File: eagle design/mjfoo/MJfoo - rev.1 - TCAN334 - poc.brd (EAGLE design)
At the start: 35 x 35 mm, 19 parts, among them IC202 LDK320AM33R, IC302 STM32F042G6U6, IC401 TCAN334, J1 CAN, J2 Power Supply

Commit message: - updated MJfoo to rev. 1a
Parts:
- added 3V3: 3V3, pinhead:1X02
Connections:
- net 3V3: now also 3V3.2
- net GND: now also 3V3.1
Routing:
- net 3V3: track 39.9 -> 46.0 mm
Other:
- board text added: "MJfoo POC ejovrh rev.1a"
- board text removed: "MJfoo POC ejovrh rev.1"
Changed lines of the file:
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@@
 <wire x1="32" y1="32" x2="3" y2="32" width="0.1524" layer="49"/>
 <text x="4" y="9.25" locked="yes" size="1" layer="29" font="vector" ratio="12" rot="R90" align="center">MJfoo POC
-ejovrh rev.1</text>
+ejovrh rev.1a</text>
 <wire x1="34" y1="32" x2="34" y2="3" width="2" layer="29" locked="yes"/>
 <wire x1="34" y1="3" x2="32" y2="1" width="2" layer="29" curve="-90" locked="yes"/>
@@
 <attribute name="VALUE" x="27.54" y="32.925" size="1.27" layer="27" rot="R180"/>
 </element>
+<element name="3V3" library="pinhead" library_urn="urn:adsk.eagle:library:325" package="1X02" package3d_urn="urn:adsk.eagle:package:22435/2" value="3V3" x="13" y="27" smashed="yes" rot="R270">
+<attribute name="NAME" x="13" y="23.75" size="1" layer="25" align="center"/>
+<attribute name="POPULARITY" value="98" x="13" y="27" size="1.778" layer="27" rot="R270" display="off"/>
+<attribute name="VALUE" x="9.825" y="29.54" size="1.27" layer="27" rot="R270"/>
+</element>
 </elements>
 <signals>
@@
 <contactref element="C401" pad="2"/>
 <via x="8.875" y="24.875" extent="1-16" drill="0.35"/>
+<contactref element="3V3" pad="1"/>
 </signal>
 <signal name="BAT+" class="1">
@@
 <wire x1="9.125" y1="22.88" x2="12.975" y2="22.88" width="0.25" layer="16"/>
 <wire x1="9.125" y1="22.025" x2="9.125" y2="22.88" width="0.25" layer="16"/>
-<wire x1="12.975" y1="20.875" x2="12.975" y2="22.75" width="0.25" layer="16"/>
-<wire x1="12.975" y1="22.75" x2="12.975" y2="22.88" width="0.25" layer="16"/>
+<wire x1="12.975" y1="20.875" x2="12.975" y2="22.88" width="0.25" layer="16"/>
 <wire x1="18.65" y1="24.98" x2="18.75" y2="24.88" width="0.25" layer="16"/>
 <wire x1="18.75" y1="24.88" x2="18.75" y2="22.88" width="0.25" layer="16"/>
@@
 <wire x1="18.65" y1="25.08" x2="18.75" y2="24.98" width="0.25" layer="1"/>
 <wire x1="18.65" y1="24.98" x2="18.75" y2="24.98" width="0.25" layer="16"/>
-<wire x1="12.975" y1="22.75" x2="12.975" y2="22.75" width="0.25" layer="16"/>
+<contactref element="3V3" pad="2"/>
+<wire x1="13" y1="25.73" x2="13.275" y2="26.005" width="0.25" layer="1"/>
+<wire x1="18.45" y1="25.33" x2="17.775" y2="26.005" width="0.25" layer="1"/>
+<wire x1="18.45" y1="25.33" x2="18.45" y2="25.08" width="0.25" layer="1"/>
+<wire x1="13.275" y1="26.005" x2="17.775" y2="26.005" width="0.25" layer="1"/>
 </signal>
 <signal name="SYS_SWDIO" class="3">

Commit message: - unified values of passive elements to a common format
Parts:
- C202: value 1μF / 10V -> 1uF / 10V
- C207: value 1μF -> 1uF / 10V
- C301, C305, C307: value 0.1u -> 0.1uF / 10V
- C304: value 1u -> 1uF / 10V
- C401: value 47nF -> 47nF / 10V
- C405: value 0.1μF -> 0.1uF / 10V
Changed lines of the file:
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@@
 </autorouter>
 <elements>
-<element name="C202" library="rcl" library_urn="urn:adsk.eagle:library:334" package="C0402" package3d_urn="urn:adsk.eagle:package:23626/2" value="1μF / 10V" x="18" y="27.48" locked="yes" smashed="yes" rot="MR0">
+<element name="C202" library="rcl" library_urn="urn:adsk.eagle:library:334" package="C0402" package3d_urn="urn:adsk.eagle:package:23626/2" value="1uF / 10V" x="18" y="27.48" locked="yes" smashed="yes" rot="MR0">
 <attribute name="NAME" x="18" y="28.48" locked="yes" size="0.5" layer="26" rot="MR0" align="center"/>
 <attribute name="POPULARITY" value="18" x="18" y="27.48" locked="yes" size="1.778" layer="28" rot="MR0" display="off"/>
@@
 <attribute name="VALUE" x="18" y="27.48" locked="yes" size="1.27" layer="28" rot="MR0"/>
 </element>
-<element name="C207" library="rcl" library_urn="urn:adsk.eagle:library:334" package="C0402" package3d_urn="urn:adsk.eagle:package:23626/2" value="1μF" x="18" y="24.98" locked="yes" smashed="yes" rot="MR180">
+<element name="C207" library="rcl" library_urn="urn:adsk.eagle:library:334" package="C0402" package3d_urn="urn:adsk.eagle:package:23626/2" value="1uF / 10V" x="18" y="24.98" locked="yes" smashed="yes" rot="MR180">
 <attribute name="NAME" x="18" y="23.98" locked="yes" size="0.5" layer="26" rot="MR180" align="center"/>
 <attribute name="POPULARITY" value="18" x="18" y="24.98" locked="yes" size="1.778" layer="28" rot="MR180" display="off"/>
@@
 <attribute name="VALUE" x="18" y="24.98" locked="yes" size="1.27" layer="28" rot="MR180"/>
 </element>
-<element name="C301" library="rcl" library_urn="urn:adsk.eagle:library:334" package="C0402" package3d_urn="urn:adsk.eagle:package:23626/2" value="0.1u" x="13.625" y="20.875" locked="yes" smashed="yes" rot="MR0">
+<element name="C301" library="rcl" library_urn="urn:adsk.eagle:library:334" package="C0402" package3d_urn="urn:adsk.eagle:package:23626/2" value="0.1uF / 10V" x="13.625" y="20.875" locked="yes" smashed="yes" rot="MR0">
 <attribute name="NAME" x="13.625" y="21.875" locked="yes" size="0.5" layer="26" rot="MR0" align="center"/>
 <attribute name="POPULARITY" value="18" x="13.625" y="20.875" locked="yes" size="1.778" layer="28" rot="MR0" display="off"/>
@@
 <attribute name="VALUE" x="13.625" y="20.875" locked="yes" size="1.27" layer="28" rot="MR0"/>
 </element>
-<element name="C304" library="rcl" library_urn="urn:adsk.eagle:library:334" package="C0402" package3d_urn="urn:adsk.eagle:package:23626/2" value="1u" x="21.75" y="20" locked="yes" smashed="yes" rot="MR0">
+<element name="C304" library="rcl" library_urn="urn:adsk.eagle:library:334" package="C0402" package3d_urn="urn:adsk.eagle:package:23626/2" value="1uF / 10V" x="21.75" y="20" locked="yes" smashed="yes" rot="MR0">
 <attribute name="NAME" x="21.75" y="21" locked="yes" size="0.5" layer="26" rot="MR0" align="center"/>
 <attribute name="POPULARITY" value="18" x="21.75" y="20" locked="yes" size="1.778" layer="28" rot="MR0" display="off"/>
@@
 <attribute name="VALUE" x="21.75" y="20" locked="yes" size="1.27" layer="28" rot="MR0"/>
 </element>
-<element name="C305" library="rcl" library_urn="urn:adsk.eagle:library:334" package="C0402" package3d_urn="urn:adsk.eagle:package:23626/2" value="0.1u" x="13.625" y="19.625" locked="yes" smashed="yes" rot="MR0">
+<element name="C305" library="rcl" library_urn="urn:adsk.eagle:library:334" package="C0402" package3d_urn="urn:adsk.eagle:package:23626/2" value="0.1uF / 10V" x="13.625" y="19.625" locked="yes" smashed="yes" rot="MR0">
 <attribute name="NAME" x="13.625" y="18.625" locked="yes" size="0.5" layer="26" rot="MR0" align="center"/>
 <attribute name="POPULARITY" value="18" x="13.625" y="19.625" locked="yes" size="1.778" layer="28" rot="MR0" display="off"/>
@@
 <attribute name="VALUE" x="13.625" y="19.625" locked="yes" size="1.27" layer="28" rot="MR0"/>
 </element>
-<element name="C307" library="rcl" library_urn="urn:adsk.eagle:library:334" package="C0402" package3d_urn="urn:adsk.eagle:package:23626/2" value="0.1u" x="3.875" y="16.875" locked="yes" smashed="yes" rot="MR90">
+<element name="C307" library="rcl" library_urn="urn:adsk.eagle:library:334" package="C0402" package3d_urn="urn:adsk.eagle:package:23626/2" value="0.1uF / 10V" x="3.875" y="16.875" locked="yes" smashed="yes" rot="MR90">
 <attribute name="NAME" x="2.875" y="16.875" locked="yes" size="0.5" layer="26" rot="MR90" align="center"/>
 <attribute name="POPULARITY" value="18" x="3.875" y="16.875" locked="yes" size="1.778" layer="28" rot="MR90" display="off"/>
@@
 <attribute name="VALUE" x="3.875" y="16.875" locked="yes" size="1.27" layer="28" rot="MR90"/>
 </element>
-<element name="C405" library="rcl" library_urn="urn:adsk.eagle:library:334" package="C0402" package3d_urn="urn:adsk.eagle:package:23626/2" value="0.1μF" x="9.125" y="21.375" locked="yes" smashed="yes" rot="MR270">
+<element name="C405" library="rcl" library_urn="urn:adsk.eagle:library:334" package="C0402" package3d_urn="urn:adsk.eagle:package:23626/2" value="0.1uF / 10V" x="9.125" y="21.375" locked="yes" smashed="yes" rot="MR270">
 <attribute name="NAME" x="8.125" y="21.375" locked="yes" size="0.5" layer="26" rot="MR270" align="center"/>
 <attribute name="POPULARITY" value="18" x="9.125" y="21.375" locked="yes" size="1.778" layer="28" rot="MR270" display="off"/>
@@
 <attribute name="VALUE" x="20.0086" y="28.9641" locked="yes" size="1.27" layer="27" rot="R180"/>
 </element>
-<element name="C401" library="rcl" library_urn="urn:adsk.eagle:library:334" package="C0402" package3d_urn="urn:adsk.eagle:package:23626/2" value="47nF" x="8.875" y="27" smashed="yes" rot="MR270">
+<element name="C401" library="rcl" library_urn="urn:adsk.eagle:library:334" package="C0402" package3d_urn="urn:adsk.eagle:package:23626/2" value="47nF / 10V" x="8.875" y="27" smashed="yes" rot="MR270">
 <attribute name="NAME" x="8.865" y="25.24" size="0.5" layer="26" rot="MR180" align="center"/>
 <attribute name="POPULARITY" value="18" x="8.875" y="27" size="1.778" layer="28" rot="MR270" display="off"/>

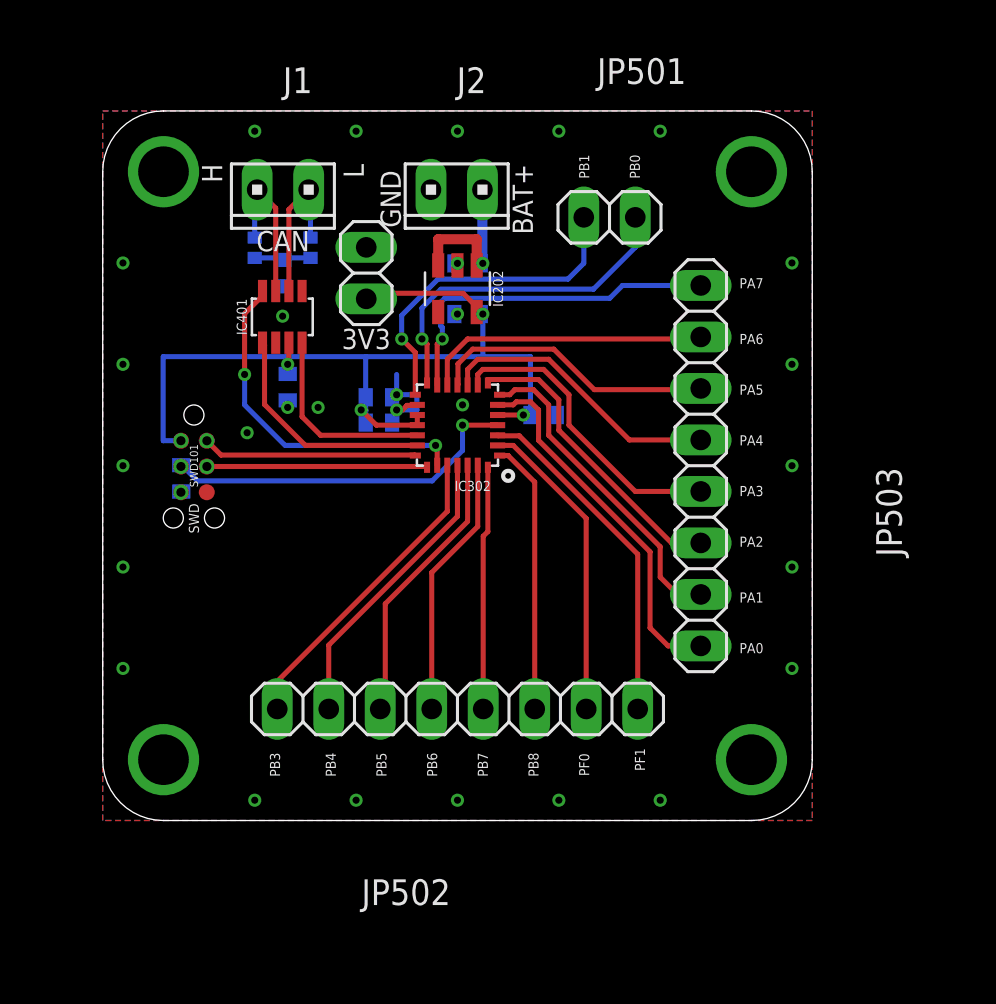
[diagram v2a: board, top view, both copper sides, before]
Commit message: - new programming adapter
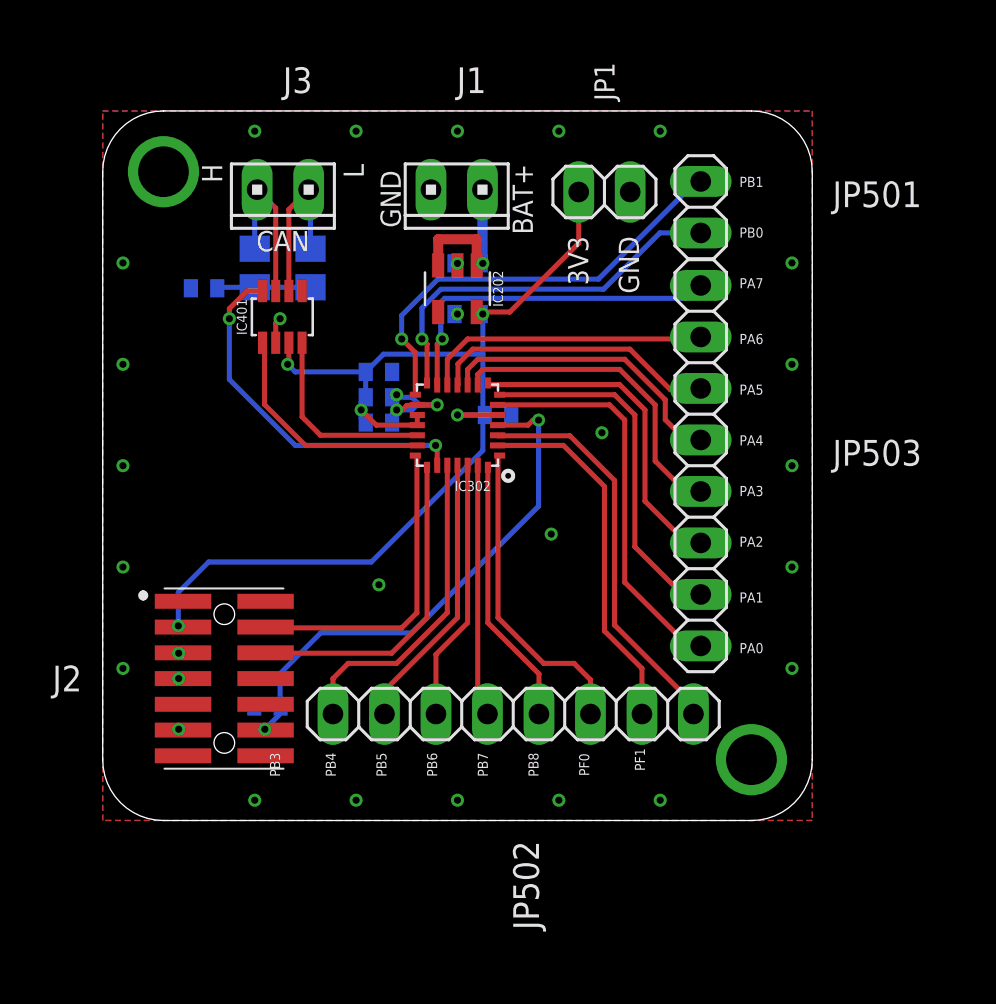
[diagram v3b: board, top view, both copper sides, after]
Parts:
- removed 3V3: 3V3, pinhead:1X02
- removed SWD101: TC2030-NL, tag-connect:TC2030-NL
- added J3: CAN, con-amp:10X02MTA
- added JP1: 3V3, pinhead:1X02
- J1: value CAN -> Power Supply
- J2: value Power Supply -> FTSH-107-01-L-DV-K-A; device con-amp:10X02MTA -> STM32 JTAG 1.27mm 14pin header:FTSH10701LDVKA
- R401, R405: device rcl:R0402 -> rcl:R0805
- moved J2 26.7 mm to (6.00, 7.00), turned to 270 degrees
- moved C307 12.0 mm to (8.12, 5.62), turned to 180 degrees
- moved J1 8.57 mm to (17.5, 31.1)
- moved C405 4.56 mm to (13.6, 22.1), turned to 180 degrees
- moved JP501 4.53 mm to (29.5, 30.2), turned to 90 degrees
- moved C401 3.95 mm to (5.00, 26.2), turned to 0 degrees
- moved JP502 2.76 mm to (20.2, 5.25)
- moved C304 2.25 mm to (19.5, 20.0)
- moved R401 1.00 mm to (7.50, 27.2)
- moved R405 1.00 mm to (10.2, 27.2)
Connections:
- net 3V3: now also J2.3, JP1.2; no longer 3V3.2, SWD101.1_TVCC
- net BAT+: now also J1.2; no longer J2.2
- net CAN_H: now also J3.1; no longer J1.1
- net CAN_L: now also J3.2; no longer J1.2
- net GND: now also J1.1, J2.11, J2.5, J2.7, JP1.1; no longer 3V3.1, J2.1, SWD101.5_GND
- net SYS_NRST: now also J2.12; no longer SWD101.3_T_NRST
- net SYS_SWCLK: now also J2.6; no longer SWD101.4_T_SWCLK
- net SYS_SWDIO: now also J2.4; no longer SWD101.2_T_SWDIO
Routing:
- net 3V3: track 46.0 -> 56.9 mm
- net SYS_NRST: track 17.9 -> 25.7 mm
- net SYS_SWCLK: track 10.9 -> 16.1 mm, vias 1 -> 0
- net PB1: track 16.5 -> 21.7 mm
- net SYS_SWDIO: track 10.6 -> 15.6 mm, vias 1 -> 0
- net GND: track 6.33 -> 9.33 mm, vias 34 -> 31
- net PF1: track 17.0 -> 19.8 mm
- net PF0: track 15.3 -> 18.1 mm
- net PB8: track 13.5 -> 15.6 mm
- net PB0: track 17.0 -> 19.1 mm
- net PA1: track 16.0 -> 17.8 mm
- net CAN_INFRA:SPLIT: track 2.83 -> 4.62 mm
- net PA0: track 18.1 -> 19.7 mm
- net PA2: track 14.9 -> 16.4 mm
- net PB7: track 12.0 -> 13.2 mm
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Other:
- board text added: "3V3"
